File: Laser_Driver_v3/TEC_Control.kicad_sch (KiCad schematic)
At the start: 49 parts, among them Q10 IRF9540N, Q11 IRLB8721PBF, Q12 IRF9540N, Q13 IRLB8721PBF, Q14 IRF9540N, Q15 IRLB8721PBF, Q16 IRF9540N, Q9 IRLB8721PBF, U18 OPA192IDR, U19 OPA192IDR, U20 OPA192IDR, U21 OPA551U, U22 OPA551U

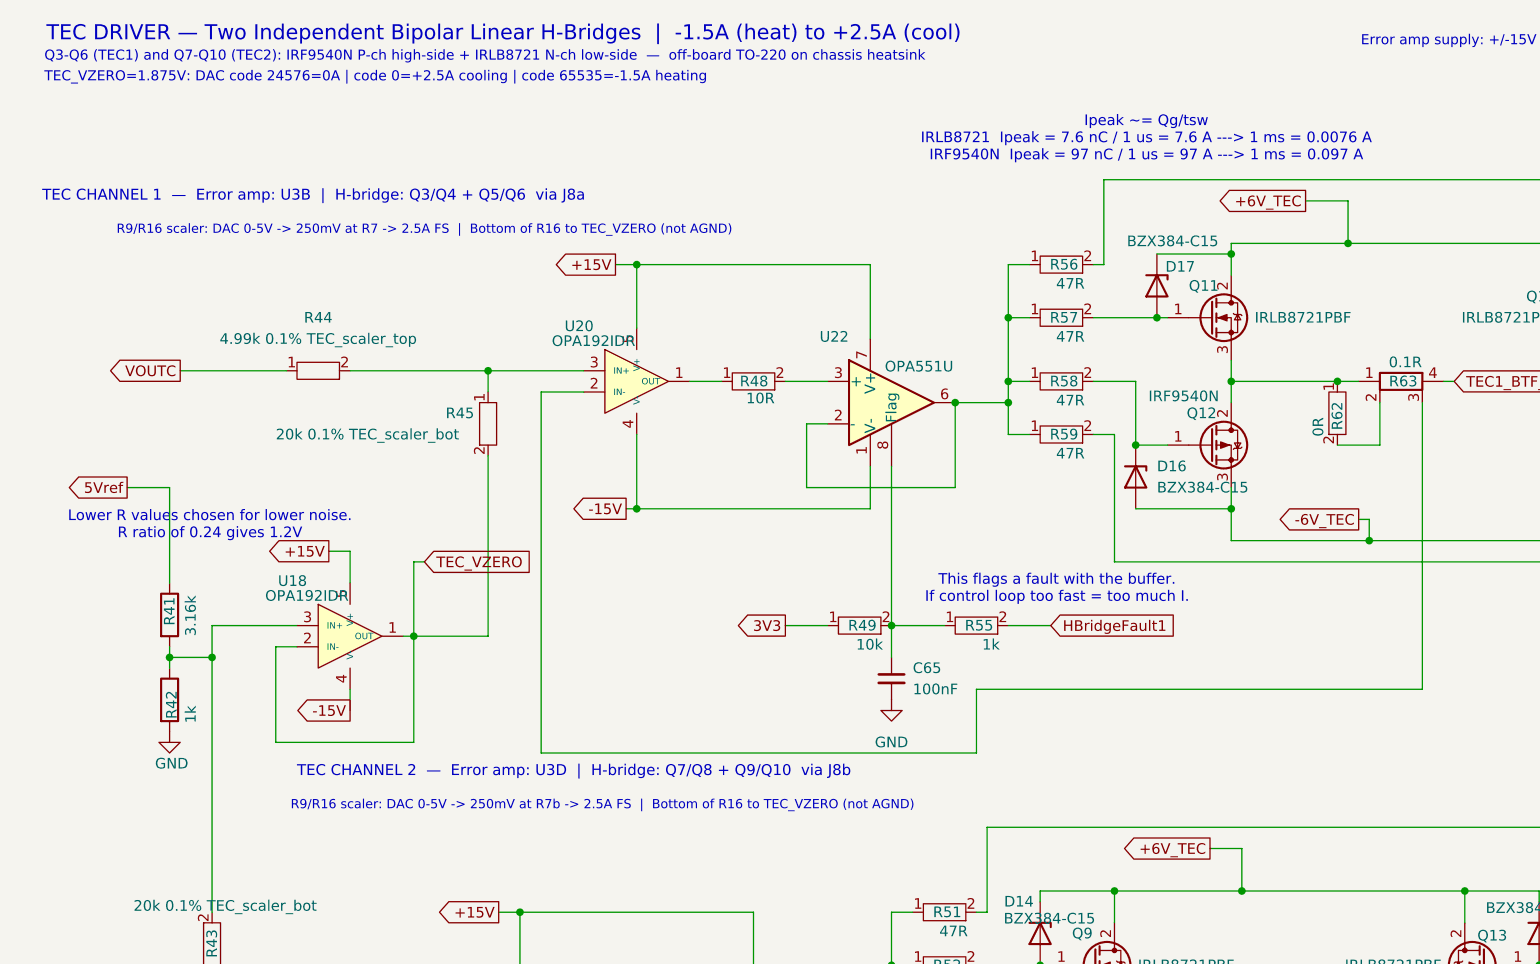
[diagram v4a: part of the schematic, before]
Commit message: 6 V supply. Annotations. Teensy zero current.
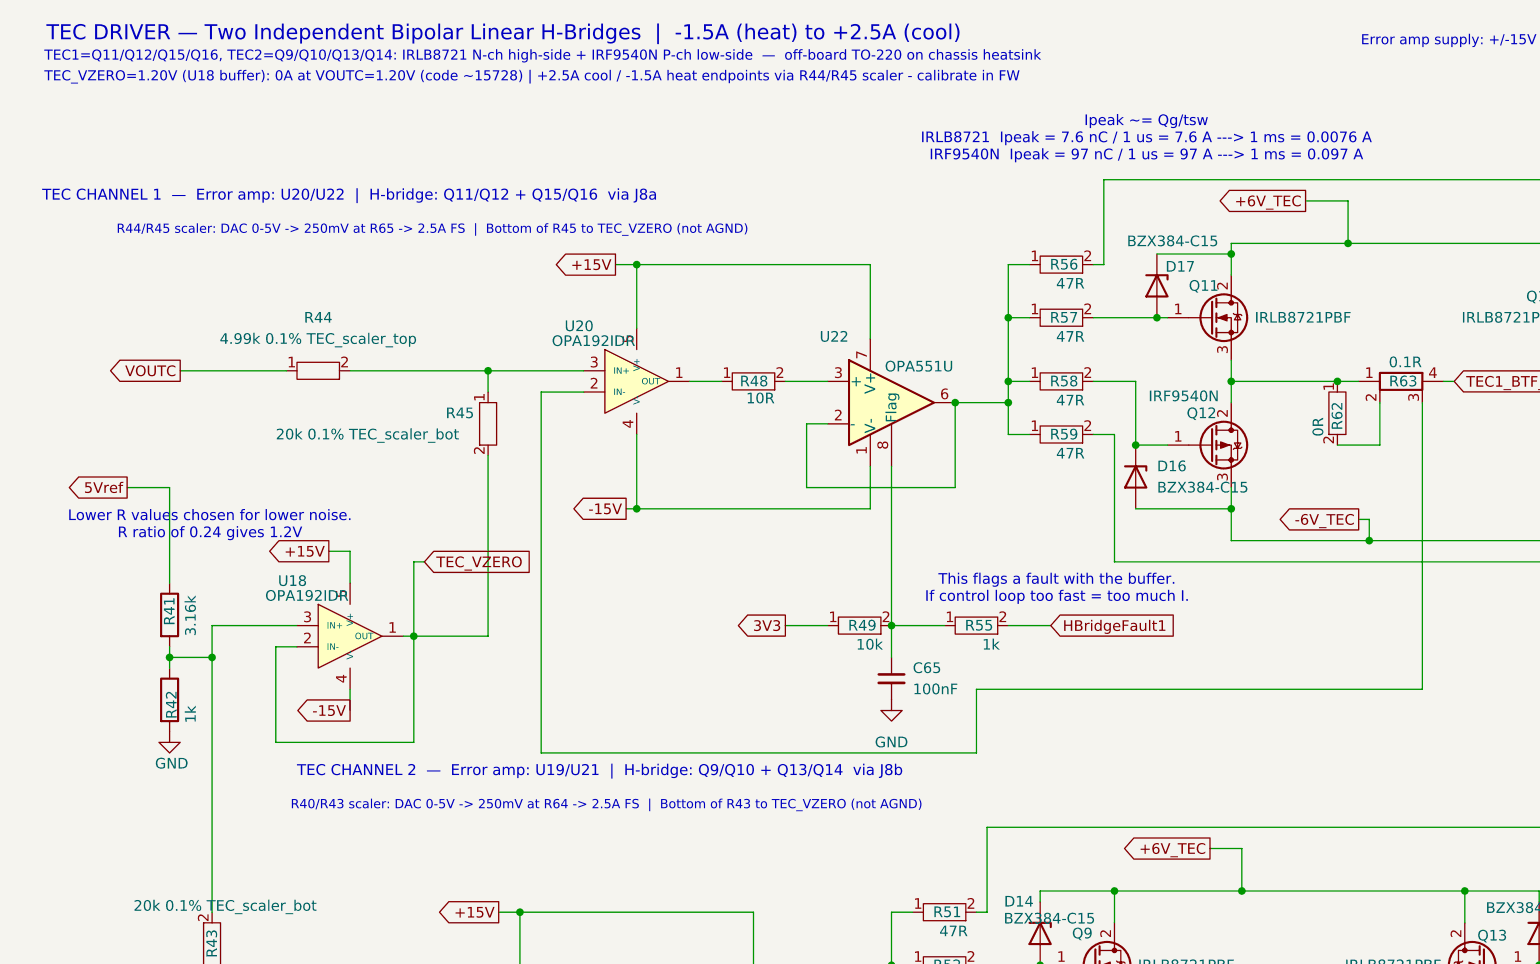
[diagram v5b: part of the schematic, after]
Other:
- note added: "R40/R43 scaler: DAC 0-5V -> 250mV at R64 -> 2.5A FS | Bottom of R43 to TEC_VZERO (not AGND)"
- note added: "R44/R45 scaler: DAC 0-5V -> 250mV at R65 -> 2.5A FS | Bottom of R45 to TEC_VZERO (not AGND)"
- note added: "TEC CHANNEL 1 — Error amp: U20/U22 | H-bridge: Q11/Q12 + Q15/Q16 via J8a"
- note added: "TEC CHANNEL 2 — Error amp: U19/U21 | H-bridge: Q9/Q10 + Q13/Q14 via J8b"
- note added: "TEC1=Q11/Q12/Q15/Q16, TEC2=Q9/Q10/Q13/Q14: IRLB8721 N-ch high-side + IRF9540N P-ch low-side — off-board TO-220 on chassis heatsink"
- note added: "TEC_VZERO=1.20V (U18 buffer): 0A at VOUTC=1.20V (code ~15728) | +2.5A cool / -1.5A heat endpoints via R44/R45 scaler - calibrate in FW"
- note removed: "Q3-Q6 (TEC1) and Q7-Q10 (TEC2): IRF9540N P-ch high-side + IRLB8721 N-ch low-side — off-board TO-220 on chassis heatsink"
- note removed: "R9/R16 scaler: DAC 0-5V -> 250mV at R7 -> 2.5A FS | Bottom of R16 to TEC_VZERO (not AGND)"
- note removed: "R9/R16 scaler: DAC 0-5V -> 250mV at R7b -> 2.5A FS | Bottom of R16 to TEC_VZERO (not AGND)"
- note removed: "TEC CHANNEL 1 — Error amp: U3B | H-bridge: Q3/Q4 + Q5/Q6 via J8a"
- note removed: "TEC CHANNEL 2 — Error amp: U3D | H-bridge: Q7/Q8 + Q9/Q10 via J8b"
- note removed: "TEC_VZERO=1.875V: DAC code 24576=0A | code 0=+2.5A cooling | code 65535=-1.5A heating"
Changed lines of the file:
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@@
 	(generator_version "10.0")
 	(paper "A4")
-	(text "Q3-Q6 (TEC1) and Q7-Q10 (TEC2): IRF9540N P-ch high-side + IRLB8721 N-ch low-side  —  off-board TO-220 on chassis heatsink"
+	(text "TEC1=Q11/Q12/Q15/Q16, TEC2=Q9/Q10/Q13/Q14: IRLB8721 N-ch high-side + IRF9540N P-ch low-side  —  off-board TO-220 on chassis heatsink"
 		(exclude_from_sim no)
 		(at 16.764 18.352 0)
@@
 		)
 	)
-	(text "TEC CHANNEL 2  —  Error amp: U3D  |  H-bridge: Q7/Q8 + Q9/Q10  via J8b"
+	(text "TEC CHANNEL 2  —  Error amp: U19/U21  |  H-bridge: Q9/Q10 + Q13/Q14  via J8b"
 		(exclude_from_sim no)
 		(at 46.99 103.886 0)
@@
 		)
 	)
-	(text "R9/R16 scaler: DAC 0-5V -> 250mV at R7 -> 2.5A FS  |  Bottom of R16 to TEC_VZERO (not AGND)"
+	(text "R44/R45 scaler: DAC 0-5V -> 250mV at R65 -> 2.5A FS  |  Bottom of R45 to TEC_VZERO (not AGND)"
 		(exclude_from_sim no)
 		(at 25.4 39.116 0)
@@
 		)
 	)
-	(text "TEC_VZERO=1.875V: DAC code 24576=0A | code 0=+2.5A cooling | code 65535=-1.5A heating"
+	(text "TEC_VZERO=1.20V (U18 buffer): 0A at VOUTC=1.20V (code ~15728) | +2.5A cool / -1.5A heat endpoints via R44/R45 scaler - calibrate in FW"
 		(exclude_from_sim no)
 		(at 16.764 20.828 0)
@@
 		)
 	)
-	(text "R9/R16 scaler: DAC 0-5V -> 250mV at R7b -> 2.5A FS  |  Bottom of R16 to TEC_VZERO (not AGND)"
+	(text "R40/R43 scaler: DAC 0-5V -> 250mV at R64 -> 2.5A FS  |  Bottom of R43 to TEC_VZERO (not AGND)"
 		(exclude_from_sim no)
 		(at 46.228 107.95 0)
@@
 		)
 	)
-	(text "TEC CHANNEL 1  —  Error amp: U3B  |  H-bridge: Q3/Q4 + Q5/Q6  via J8a"
+	(text "TEC CHANNEL 1  —  Error amp: U20/U22  |  H-bridge: Q11/Q12 + Q15/Q16  via J8a"
 		(exclude_from_sim no)
 		(at 16.51 35.052 0)

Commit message: Updated the RF modulation implementation.
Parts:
- renumbered Q9 to Q11, Q10 to Q12, Q11 to Q13, Q12 to Q14, Q13 to Q15, Q14 to Q16, Q15 to Q17, Q16 to Q18, U18 to U17, U19 to U18, U20 to U19, U21 to U20, U22 to U21
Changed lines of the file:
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@@
 		(in_pos_files yes)
 		(dnp no)
-		(property "Reference" "Q15"
+		(property "Reference" "Q17"
 			(at 197.612 46.99 0)
 			(show_name no)
@@
 			(project "laser_driver_v3"
 				(path "/b2c3d4e5-f6a7-8901-bcde-f12345678901/06f22b47-dee6-4fbe-8e7e-6abe24fabe38"
-					(reference "Q15")
+					(reference "Q17")
 					(unit 1)
 				)
@@
 		(in_pos_files yes)
 		(dnp no)
-		(property "Reference" "#PWR020"
+		(property "Reference" "#PWR018"
 			(at 31.75 105.41 0)
 			(hide yes)
@@
 			(project "laser_driver_v3"
 				(path "/b2c3d4e5-f6a7-8901-bcde-f12345678901/06f22b47-dee6-4fbe-8e7e-6abe24fabe38"
-					(reference "#PWR020")
+					(reference "#PWR018")
 					(unit 1)
 				)
@@
 		(in_pos_files yes)
 		(dnp no)
-		(property "Reference" "U19"
+		(property "Reference" "U18"
 			(at 65.024 128.016 0)
 			(show_name no)
@@
 			(project "laser_driver_v3"
 				(path "/b2c3d4e5-f6a7-8901-bcde-f12345678901/06f22b47-dee6-4fbe-8e7e-6abe24fabe38"
-					(reference "U19")
+					(reference "U18")
 					(unit 1)
 				)
@@
 		(in_pos_files yes)
 		(dnp no)
-		(property "Reference" "Q12"
+		(property "Reference" "Q14"
 			(at 153.416 60.96 0)
 			(show_name no)
@@
 			(project "laser_driver_v3"
 				(path "/b2c3d4e5-f6a7-8901-bcde-f12345678901/06f22b47-dee6-4fbe-8e7e-6abe24fabe38"
-					(reference "Q12")
+					(reference "Q14")
 					(unit 1)
 				)
@@
 		(in_pos_files yes)
 		(dnp no)
-		(property "Reference" "Q9"
+		(property "Reference" "Q11"
 			(at 139.7 123.19 0)
 			(show_name no)
@@
 			(project "laser_driver_v3"
 				(path "/b2c3d4e5-f6a7-8901-bcde-f12345678901/06f22b47-dee6-4fbe-8e7e-6abe24fabe38"
-					(reference "Q9")
+					(reference "Q11")
 					(unit 1)
 				)
@@
 		(in_pos_files yes)
 		(dnp no)
-		(property "Reference" "U20"
+		(property "Reference" "U19"
 			(at 78.994 50.546 0)
 			(show_name no)
@@
 			(project "laser_driver_v3"
 				(path "/b2c3d4e5-f6a7-8901-bcde-f12345678901/06f22b47-dee6-4fbe-8e7e-6abe24fabe38"
-					(reference "U20")
+					(reference "U19")
 					(unit 1)
 				)
@@
 		(dnp no)
 		(fields_autoplaced yes)
-		(property "Reference" "#PWR022"
+		(property "Reference" "#PWR020"
 			(at 118.11 101.6 0)
 			(hide yes)
@@
 			(project "laser_driver_v3"
 				(path "/b2c3d4e5-f6a7-8901-bcde-f12345678901/06f22b47-dee6-4fbe-8e7e-6abe24fabe38"
-					(reference "#PWR022")
+					(reference "#PWR020")
 					(unit 1)
 				)
@@
 		(in_pos_files yes)
 		(dnp no)
-		(property "Reference" "U22"
+		(property "Reference" "U21"
 			(at 111.252 51.816 0)
 			(show_name no)
@@
 			(project "laser_driver_v3"
 				(path "/b2c3d4e5-f6a7-8901-bcde-f12345678901/06f22b47-dee6-4fbe-8e7e-6abe24fabe38"
-					(reference "U22")
+					(reference "U21")
 					(unit 1)
 				)
@@
 		(in_pos_files yes)
 		(dnp no)
-		(property "Reference" "Q11"
+		(property "Reference" "Q13"
 			(at 153.67 45.72 0)
 			(show_name no)
@@
 			(project "laser_driver_v3"
 				(path "/b2c3d4e5-f6a7-8901-bcde-f12345678901/06f22b47-dee6-4fbe-8e7e-6abe24fabe38"
-					(reference "Q11")
+					(reference "Q13")
 					(unit 1)
 				)
@@
 		(in_pos_files yes)
 		(dnp no)
-		(property "Reference" "Q14"
+		(property "Reference" "Q16"
 			(at 192.024 136.398 0)
 			(show_name no)
@@
 			(project "laser_driver_v3"
 				(path "/b2c3d4e5-f6a7-8901-bcde-f12345678901/06f22b47-dee6-4fbe-8e7e-6abe24fabe38"
-					(reference "Q14")
+					(reference "Q16")
 					(unit 1)
 				)
@@
 		(in_pos_files yes)
 		(dnp no)
-		(property "Reference" "U21"
+		(property "Reference" "U20"
 			(at 97.282 129.286 0)
 			(show_name no)
@@
 			(project "laser_driver_v3"
 				(path "/b2c3d4e5-f6a7-8901-bcde-f12345678901/06f22b47-dee6-4fbe-8e7e-6abe24fabe38"
-					(reference "U21")
+					(reference "U20")
 					(unit 1)
 				)
@@
 		(in_pos_files yes)
 		(dnp no)
-		(property "Reference" "U18"
+		(property "Reference" "U17"
 			(at 44.704 81.026 0)
 			(show_name no)
@@
 			(project "laser_driver_v3"
 				(path "/b2c3d4e5-f6a7-8901-bcde-f12345678901/06f22b47-dee6-4fbe-8e7e-6abe24fabe38"
-					(reference "U18")
+					(reference "U17")
 					(unit 1)
 				)
@@
 		(dnp no)
 		(fields_autoplaced yes)
-		(property "Reference" "#PWR021"
+		(property "Reference" "#PWR019"
 			(at 104.14 179.07 0)
 			(hide yes)
@@
 			(project "laser_driver_v3"
 				(path "/b2c3d4e5-f6a7-8901-bcde-f12345678901/06f22b47-dee6-4fbe-8e7e-6abe24fabe38"
-					(reference "#PWR021")
+					(reference "#PWR019")
 					(unit 1)
 				)
@@
 		(in_pos_files yes)
 		(dnp no)
-		(property "Reference" "Q10"
+		(property "Reference" "Q12"
 			(at 139.446 138.43 0)
 			(show_name no)
@@
 			(project "laser_driver_v3"
 				(path "/b2c3d4e5-f6a7-8901-bcde-f12345678901/06f22b47-dee6-4fbe-8e7e-6abe24fabe38"
-					(reference "Q10")
+					(reference "Q12")
 					(unit 1)
 				)
@@
 		(in_pos_files yes)
 		(dnp no)
-		(property "Reference" "Q16"
+		(property "Reference" "Q18"
 			(at 208.026 58.928 0)
 			(show_name no)
@@
 			(project "laser_driver_v3"
 				(path "/b2c3d4e5-f6a7-8901-bcde-f12345678901/06f22b47-dee6-4fbe-8e7e-6abe24fabe38"
-					(reference "Q16")
+					(reference "Q18")
 					(unit 1)
 				)
@@
 		(in_pos_files yes)
 		(dnp no)
-		(property "Reference" "Q13"
+		(property "Reference" "Q15"
 			(at 191.77 123.444 0)
 			(show_name no)
@@
 			(project "laser_driver_v3"
 				(path "/b2c3d4e5-f6a7-8901-bcde-f12345678901/06f22b47-dee6-4fbe-8e7e-6abe24fabe38"
-					(reference "Q13")
+					(reference "Q15")
 					(unit 1)
 				)
